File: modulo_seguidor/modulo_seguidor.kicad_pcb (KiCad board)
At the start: 2 copper layers, 140 x 90 mm, 26 parts, among them J1 Battery, J6 puerto sensores, M1 Motor_IZQ, M2 Motor_DER, SW1 SW_Push, SW2 SW_Nidec_CAS-120A1, U1 LM7806_TO220, U2 L298N

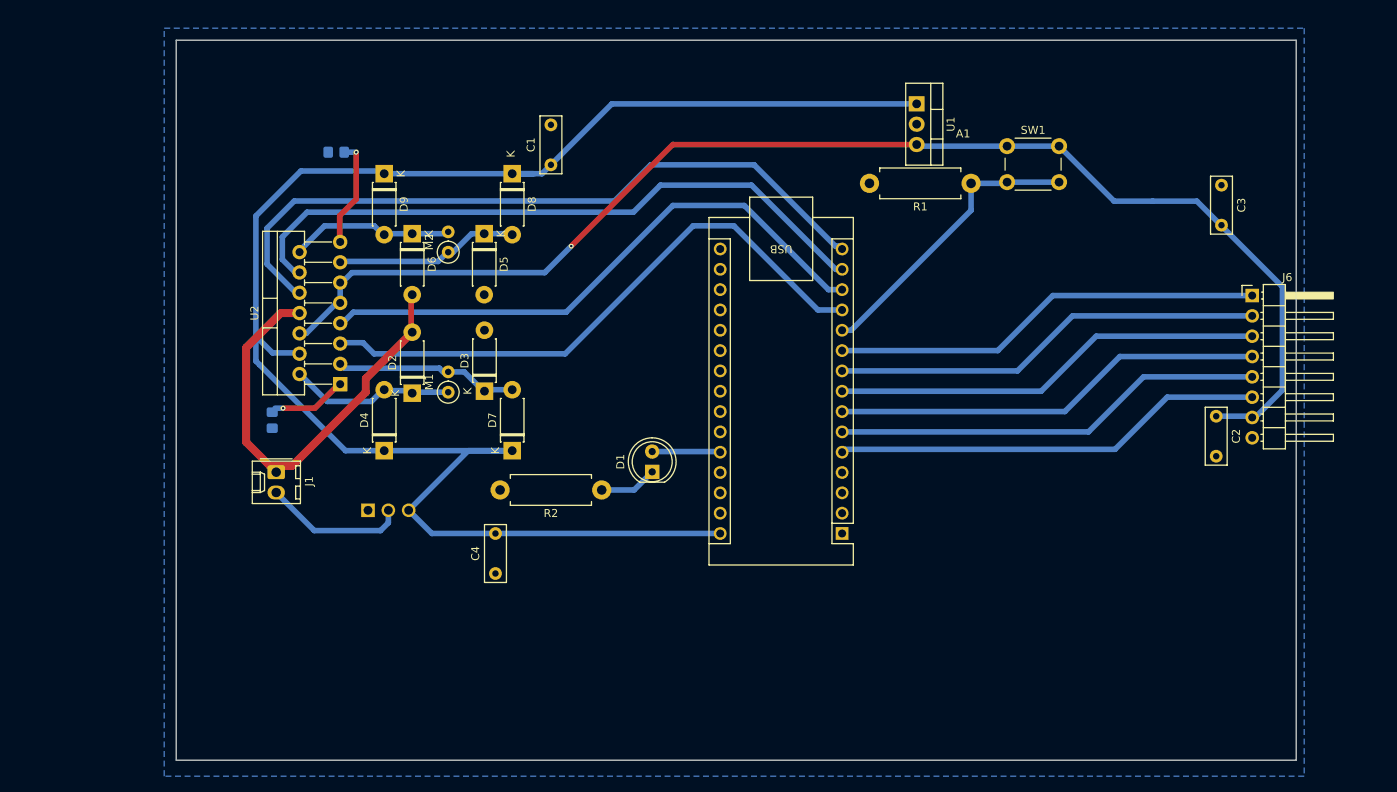
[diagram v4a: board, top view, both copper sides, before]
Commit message: feat(modulo_seguidor): Agrego boceto PCB del seguidor + puente H
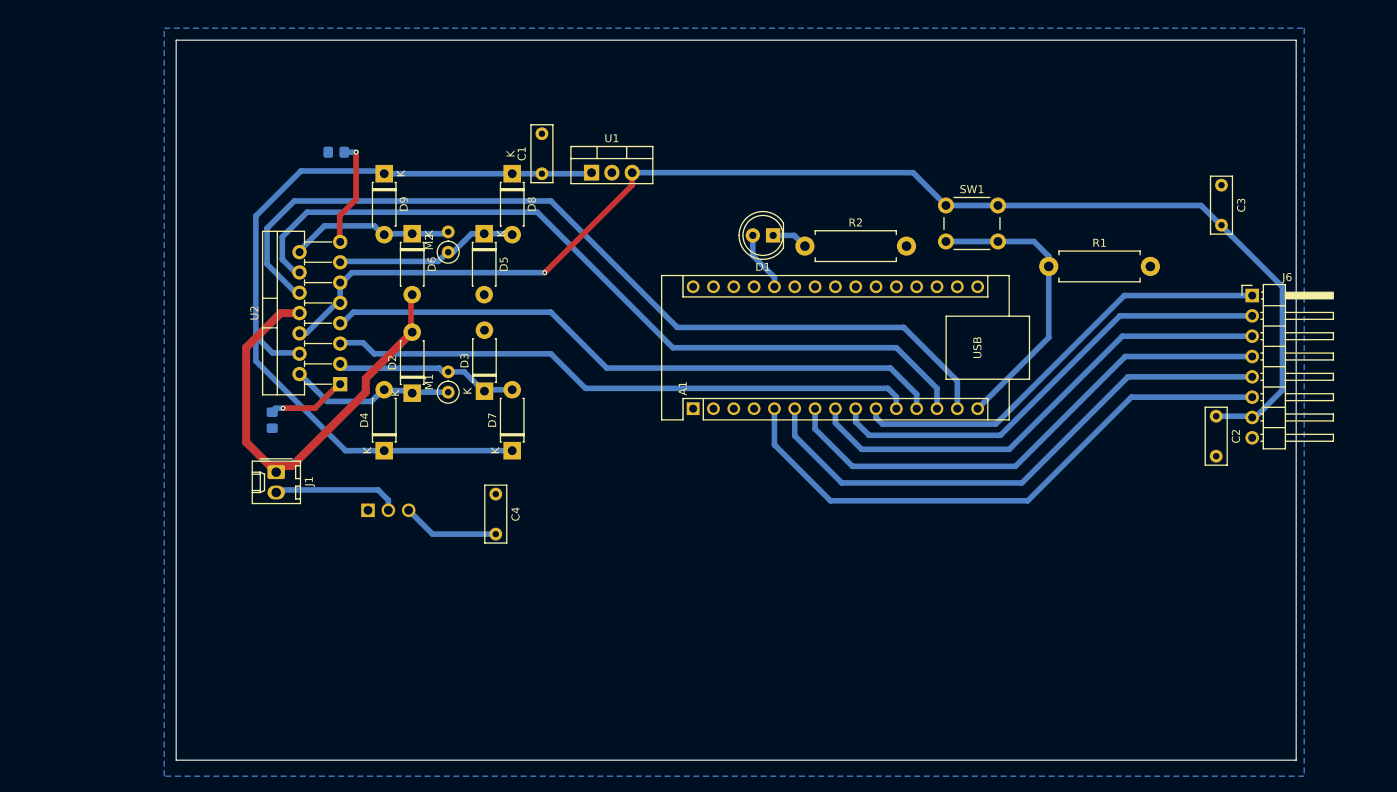
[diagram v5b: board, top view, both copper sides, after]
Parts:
- moved U1 41.5 mm to (121.9, 69.6), turned to 0 degrees
- moved R2 39.7 mm to (148.6, 78.7), turned to 0 degrees
- moved D1 33.2 mm to (144.6, 77.4), turned to 180 degrees
- moved A1 24.3 mm to (134.6, 99.1), turned to 90 degrees
- moved R1 14.2 mm to (179.1, 81.3), turned to 0 degrees
- moved SW1 10.6 mm to (166.2, 73.7)
- moved C4 9.93 mm to (109.9, 109.7), turned to -90 degrees
- moved C1 1.58 mm to (115.7, 69.7)
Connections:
- A1 pad 11: /Boton_encendido -> /Entrada PWM Motor A
- A1 pad 12: /Entrada PWM Motor A -> /Entrada DIG Motor A
- A1 pad 13: /Entrada DIG Motor A -> /Entrada DIG Motor B
- A1 pad 14: /Entrada DIG Motor B -> /Entrada PWM Motor B
- A1 pad 15: /Entrada PWM Motor B -> /Boton_encendido
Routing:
- net VCC: track 208.5 -> 117.8 mm
- net /Entrada PWM Motor B: track 89.4 -> 110.4 mm
- net /Sensor1: track 54.1 -> 72.5 mm
- net /Entrada DIG Motor B: track 82.5 -> 100.3 mm
- net /Sensor2: track 54.1 -> 68.5 mm
- net /Sensor3: track 54.1 -> 64.8 mm
- net /Sensor4: track 54.1 -> 61.1 mm
- net /Entrada DIG Motor A: track 73.2 -> 78.7 mm
- net /Sensor5: track 54.1 -> 58.1 mm
- net Salida Regulador: track 164.2 -> 161.1 mm
- net Net-(D1-K): track 7.25 -> 4.53 mm
- net Net-(J1-Pin_2): track 18.0 -> 15.9 mm
- net /Sensor6: track 54.1 -> 55.1 mm
- net Net-(A1-A7): track 8.53 -> 7.54 mm

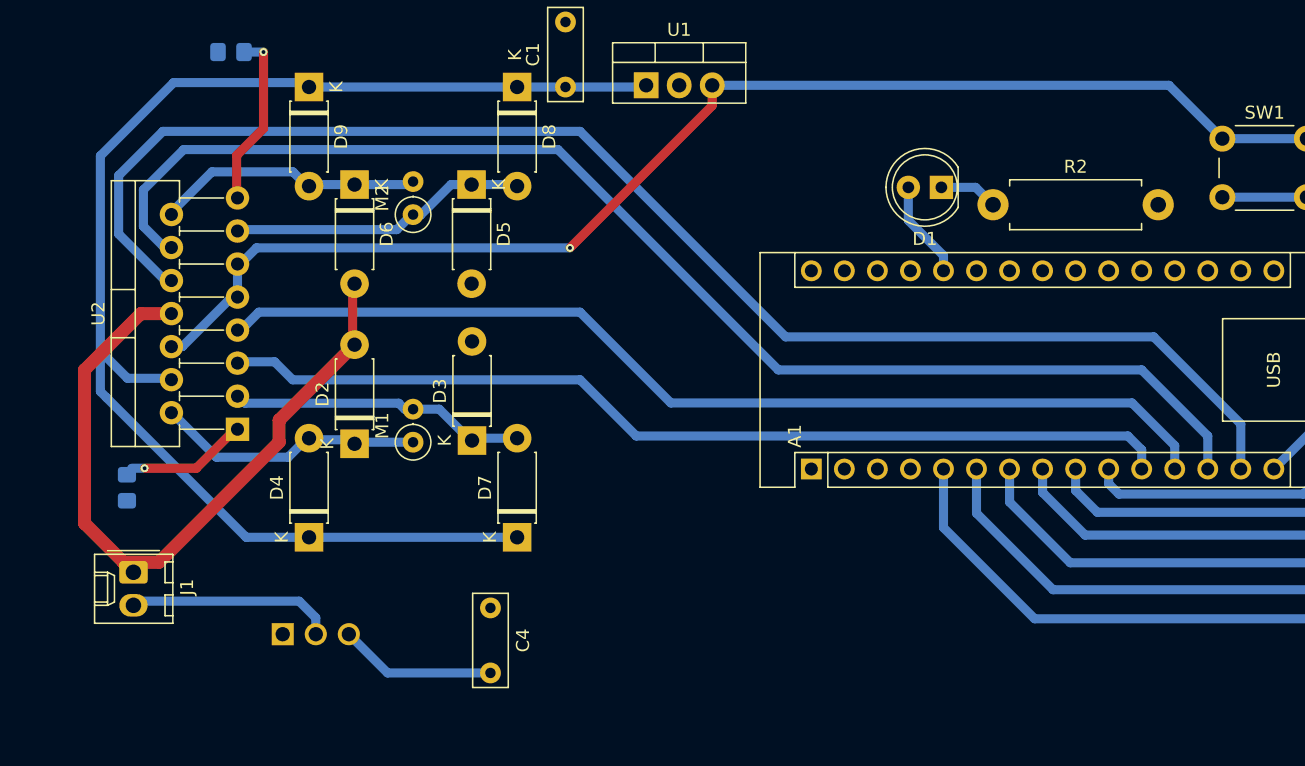
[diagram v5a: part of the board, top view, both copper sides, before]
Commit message: refactor(modulo-seguidor): Reorganizo vías y limpio carpeta de puente h
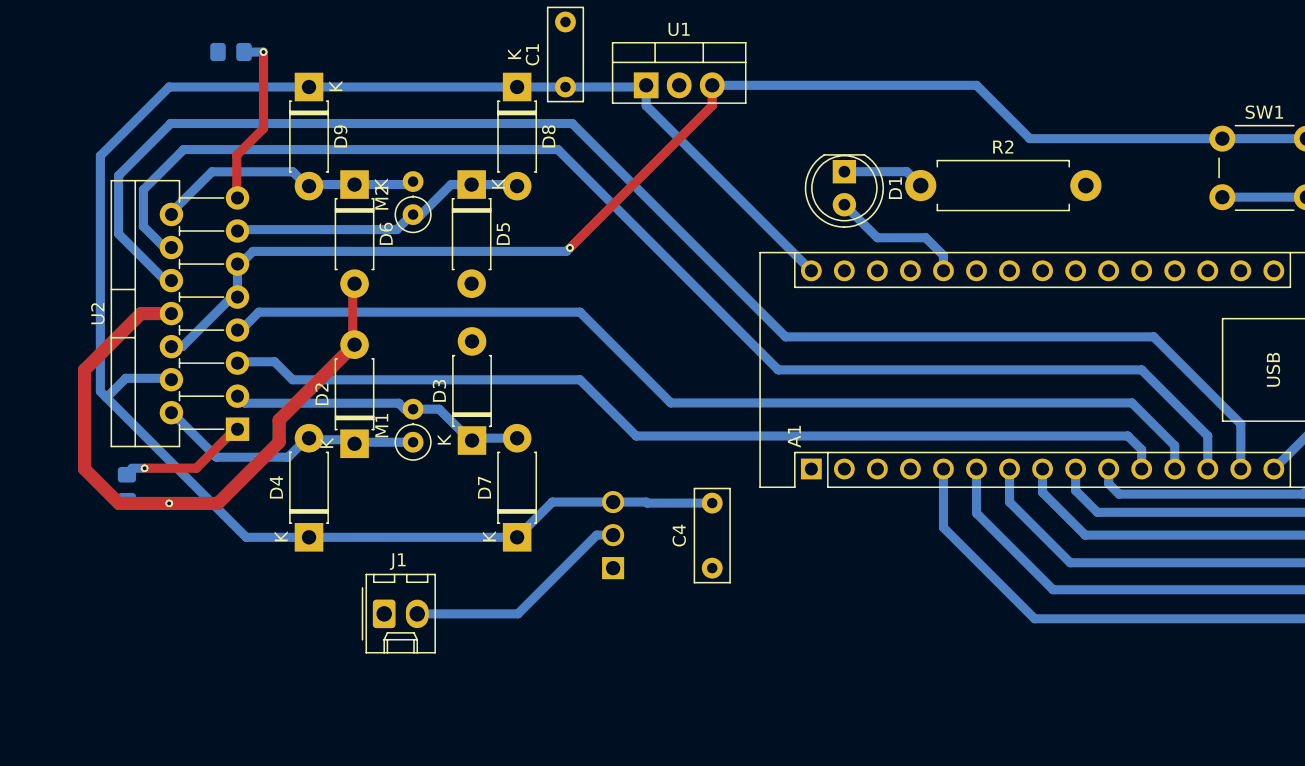
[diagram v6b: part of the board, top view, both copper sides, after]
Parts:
- moved SW2 25.9 mm to (119.4, 106.7), turned to 0 degrees
- moved J1 19.5 mm to (101.8, 110.2), turned to 0 degrees
- moved C4 17.3 mm to (127.0, 106.7), turned to 90 degrees
- moved D1 7.55 mm to (137.2, 76.2), turned to -90 degrees
- moved R2 5.75 mm to (143.0, 77.3)
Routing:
- net VCC: track 117.8 -> 140.5 mm
- net GND: track 56.5 -> 49.2 mm, vias 0 -> 1
- net Net-(A1-A7): track 7.54 -> 10.4 mm
- net Net-(D1-K): track 4.53 -> 6.31 mm
- net Net-(J1-Pin_2): track 15.9 -> 17.6 mm

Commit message: refactor!(modulo-seguidor): Modifico forma de la placa
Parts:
- R2: footprint Resistor_THT:R_Axial_DIN0411_L9.9mm_D3.6mm_P12.70mm_Horizontal -> Resistor_SMD:R_1206_3216Metric_Pad1.30x1.75mm_HandSolder; moved to B.Cu
- moved SW1 61.9 mm to (112.3, 104.1), turned to 90 degrees
- moved R1 58.1 mm to (122.7, 95.2), turned to 20 degrees
- moved C4 57.1 mm to (78.7, 76.1)
- moved A1 51.4 mm to (185.7, 93.3), turned to -90 degrees
- moved C3 40.6 mm to (203.2, 111.7), turned to 90 degrees
- moved C2 38.7 mm to (167.6, 78.7), turned to 180 degrees
- moved R2 32.0 mm to (130.5, 106.7), turned to 180 degrees
- moved D1 30.5 mm to (137.2, 106.7), turned to 0 degrees
- moved U1 28.8 mm to (106.7, 94.0)
- moved R4 26.0 mm to (72.7, 86.4)
- moved J1 25.5 mm to (109.2, 134.6), turned to 90 degrees
- moved D2 20.1 mm to (87.5, 113.3)
- moved D3 20.1 mm to (96.5, 113.0)
- moved D4 20.1 mm to (84.0, 120.5)
- moved D5 20.1 mm to (96.5, 93.4)
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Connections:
- A1 pad 11: /Entrada PWM Motor A -> /Boton_encendido
- A1 pad 12: /Entrada DIG Motor A -> /Entrada PWM Motor A
- A1 pad 13: /Entrada DIG Motor B -> /Entrada DIG Motor A
- A1 pad 14: /Entrada PWM Motor B -> /Entrada DIG Motor B
- A1 pad 15: /Boton_encendido -> /Entrada PWM Motor B
- J6 pad 1: /Sensor6 -> /Sensor1
- J6 pad 2: /Sensor5 -> /Sensor2
- J6 pad 3: /Sensor4 -> /Sensor3
- J6 pad 4: /Sensor3 -> /Sensor4
- J6 pad 5: /Sensor2 -> /Sensor5
- J6 pad 6: /Sensor1 -> /Sensor6
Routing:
- net Salida Regulador: track 161.1 -> 24.0 mm, vias 1 -> 0
- net /Entrada PWM Motor B: track 110.9 -> 0.00 mm
- net /Entrada DIG Motor B: track 100.3 -> 0.00 mm
- net /Entrada DIG Motor A: track 78.7 -> 0.00 mm
- net /Entrada PWM Motor A: track 73.9 -> 0.00 mm
- net GND: track 49.2 -> 0.05 mm, vias 1 -> 0
- net VCC: track 140.5 -> 178.8 mm
- net /Sensor1: track 72.5 -> 40.0 mm
- net Net-(A1-A7): track 10.4 -> 37.8 mm
- net /Sensor2: track 68.5 -> 42.3 mm
- net /Boton_encendido: track 36.3 -> 58.0 mm
- net /Sensor3: track 64.8 -> 46.6 mm
- net /Sensor4: track 61.1 -> 49.6 mm
- net /Sensor5: track 58.1 -> 52.0 mm
- net Net-(U2-SENSE_B): track 13.5 -> 11.5 mm
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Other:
- board size 140 x 90 mm -> 150 x 76 mm

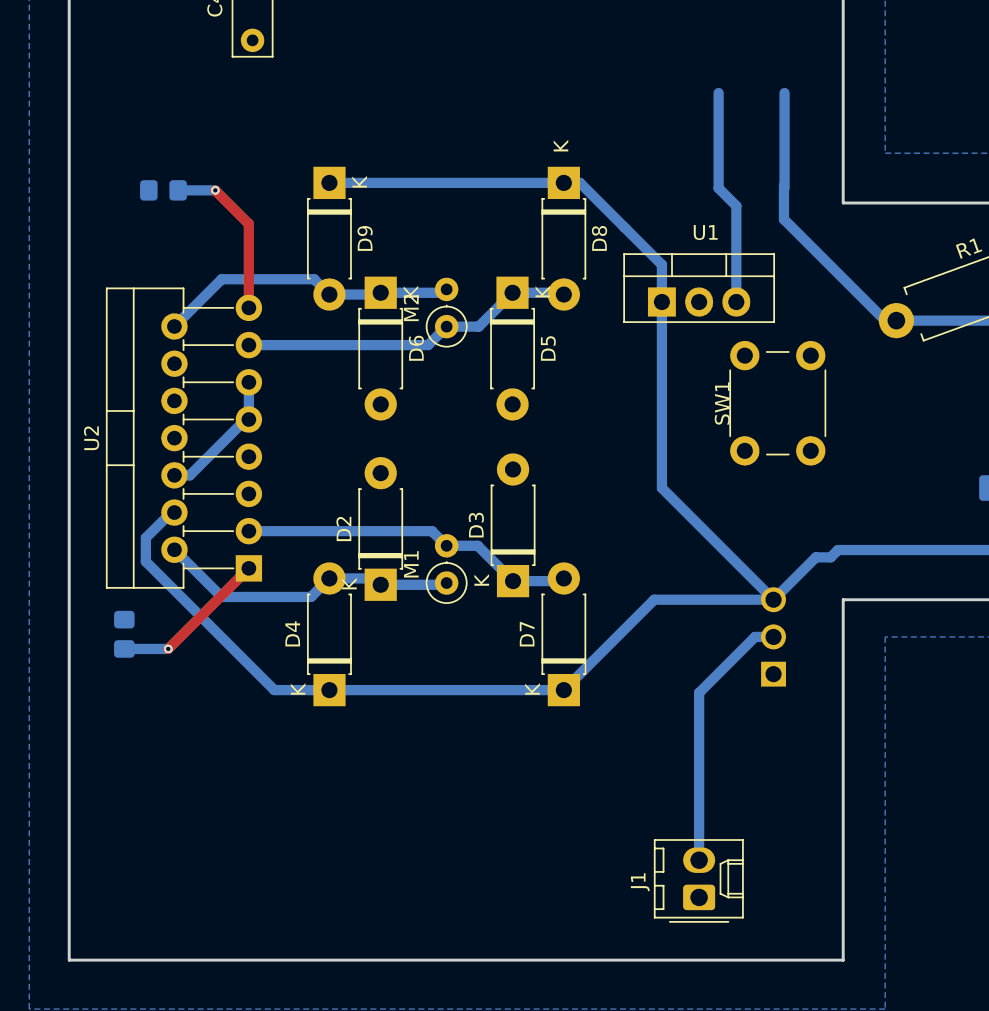
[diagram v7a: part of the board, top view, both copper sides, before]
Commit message: refactor(modulo-seguidor): Continuo el boceto de la placa
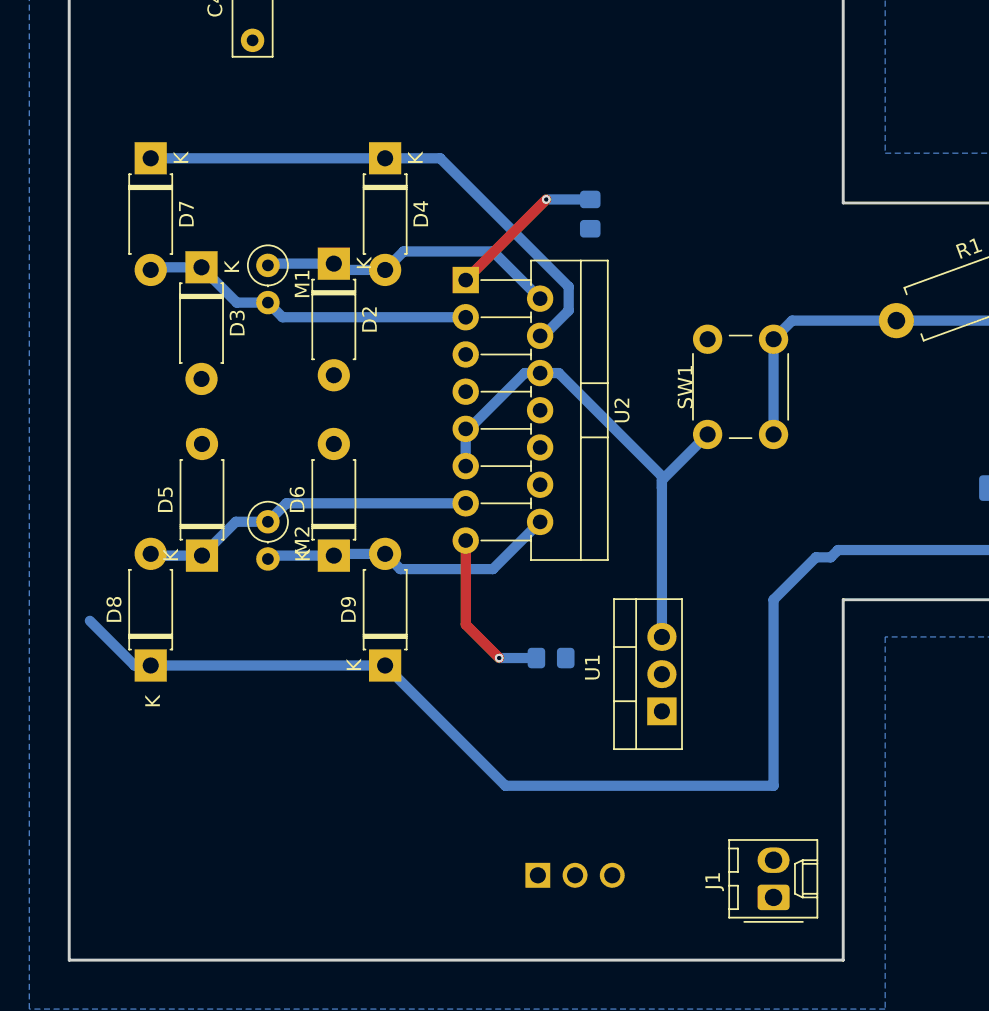
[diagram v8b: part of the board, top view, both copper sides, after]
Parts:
- moved D7 46.0 mm to (71.8, 84.2), turned to -90 degrees
- moved D8 43.4 mm to (71.8, 118.8), turned to 90 degrees
- moved R3 42.8 mm to (101.8, 88.0), turned to -90 degrees
- moved R4 41.5 mm to (99.1, 118.3), turned to 180 degrees
- moved D4 36.5 mm to (87.8, 84.2), turned to -90 degrees
- moved D9 33.2 mm to (87.8, 118.8), turned to 90 degrees
- moved D3 30.2 mm to (75.3, 91.6), turned to -90 degrees
- moved U1 27.9 mm to (106.7, 121.9), turned to 90 degrees
- moved D5 27.8 mm to (75.3, 111.3), turned to 90 degrees
- moved M1 24.9 mm to (79.8, 91.5), turned to -90 degrees
- moved U2 24.6 mm to (93.3, 92.5), turned to -90 degrees
- moved D2 22.2 mm to (84.3, 91.4), turned to -90 degrees
- moved SW2 21.2 mm to (98.2, 133.1), turned to -90 degrees
- moved D6 18.2 mm to (84.3, 111.3), turned to 90 degrees
- moved M2 18.1 mm to (79.8, 109.0), turned to -90 degrees
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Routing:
- net Net-(J1-Pin_2): track 18.1 -> 0.00 mm
- net Salida Regulador: track 24.0 -> 36.3 mm
- net VCC: track 178.8 -> 174.9 mm
- net /Boton_encendido: track 58.0 -> 54.8 mm
